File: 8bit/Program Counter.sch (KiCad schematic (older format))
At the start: 7 parts

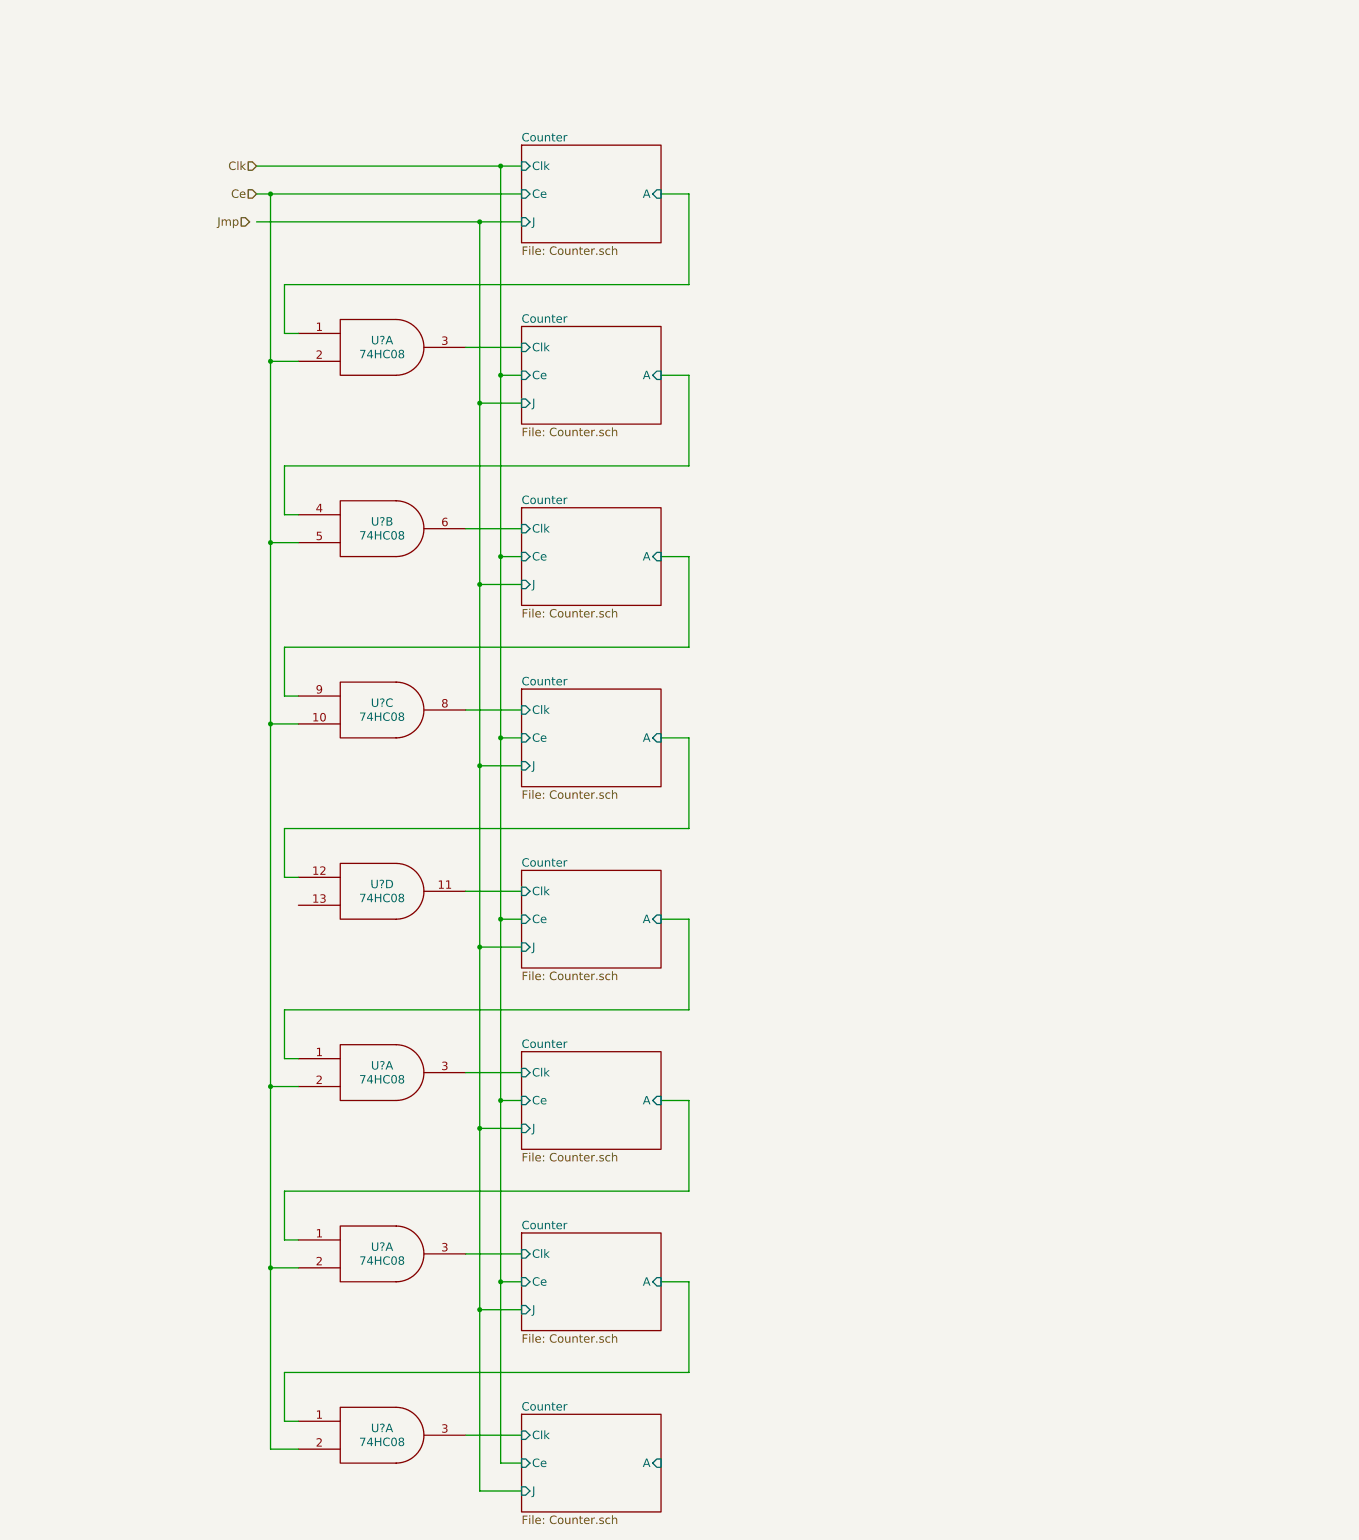
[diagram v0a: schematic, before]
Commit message: Counter mux in progress
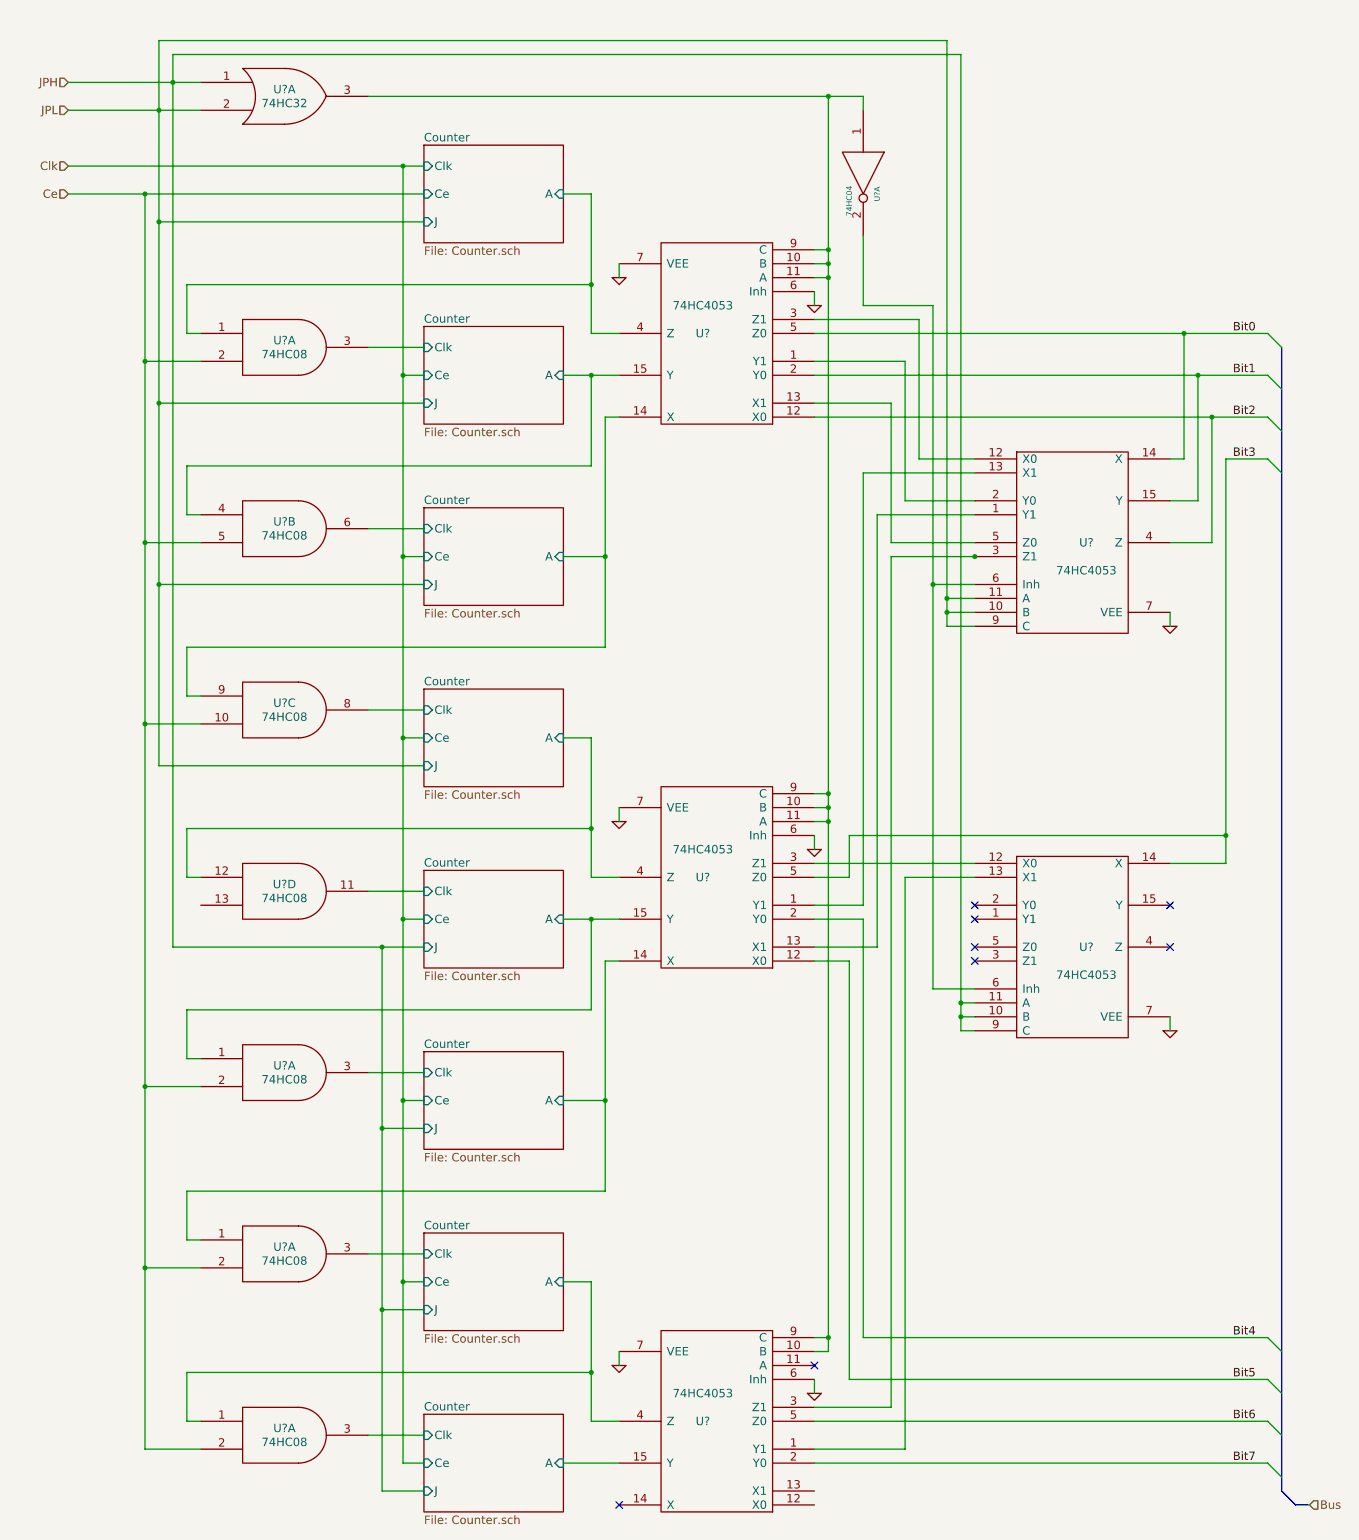
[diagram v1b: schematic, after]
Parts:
- added U?: 74HC32, symbol 74HC32
- added U?: 74HC04, symbol 74HC04
- added U? (x5): 74HC4053, symbol 74HC4053
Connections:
- net Counter/Clk is gone; now on net Counter/Clk: U?.3
- net Counter/A: now also U?.15 (Y) (x3)
- net Counter/Clk: no longer U?.3
- net GND: now also U?.6 (Inh), U?.6 (Inh), U?.6 (Inh), U?.7 (GND), U?.7 (GND), U?.7 (VEE), U?.7 (VEE), U?.7 (VEE), U?.7 (VEE), U?.7 (VEE)
- net VCC: now also U?.14 (VCC), U?.14 (VCC)
- net Counter/A: now also U?.4 (Z) (x3)
- net Counter/A: now also U?.14 (X) (x2)
- new net: U?.1, U?.10 (B), U?.10 (B), U?.10 (B), U?.11 (A), U?.11 (A), U?.3, U?.9 (C), U?.9 (C), U?.9 (C)
- new net: U?.2, U?.6 (Inh), U?.6 (Inh)
- new net: U?.1 (Y1), U?.13 (X1) (x3)
- new net: U?.12 (X0), U?.3 (Z1) (x2)
- new net: U?.1 (Y1), U?.2 (Y0)
- new net: U?.13 (X1), U?.5 (Z0)
- new net: U?.3 (Z1), U?.3 (Z1)
- new net Bit0: U?.14 (X), U?.5 (Z0)
- new net Bit1: U?.15 (Y), U?.2 (Y0)
- new net Bit2: U?.12 (X0), U?.4 (Z)
- new net Bit3: U?.14 (X), U?.5 (Z0)
- new net Bit4: U?.2 (Y0)
- new net Bit5: U?.12 (X0)
- new net Bit6: U?.5 (Z0)
- new net Bit7: U?.2 (Y0)
- new net Counter/Clk: U?.3
- new net JPH: U?.1, U?.10 (B), U?.11 (A), U?.9 (C)
- new net JPL: U?.10 (B), U?.11 (A), U?.2, U?.9 (C)
- new net VDD: U?.16 (VDD), U?.16 (VDD), U?.16 (VDD), U?.16 (VDD), U?.16 (VDD)
- new net VSS: U?.8 (VSS), U?.8 (VSS), U?.8 (VSS), U?.8 (VSS), U?.8 (VSS)
- no-connect marks 0 -> 8
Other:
- moved on the sheet: U?A, U?B, U?C, U?D

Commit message: Added tri-state buffer functionality to counter
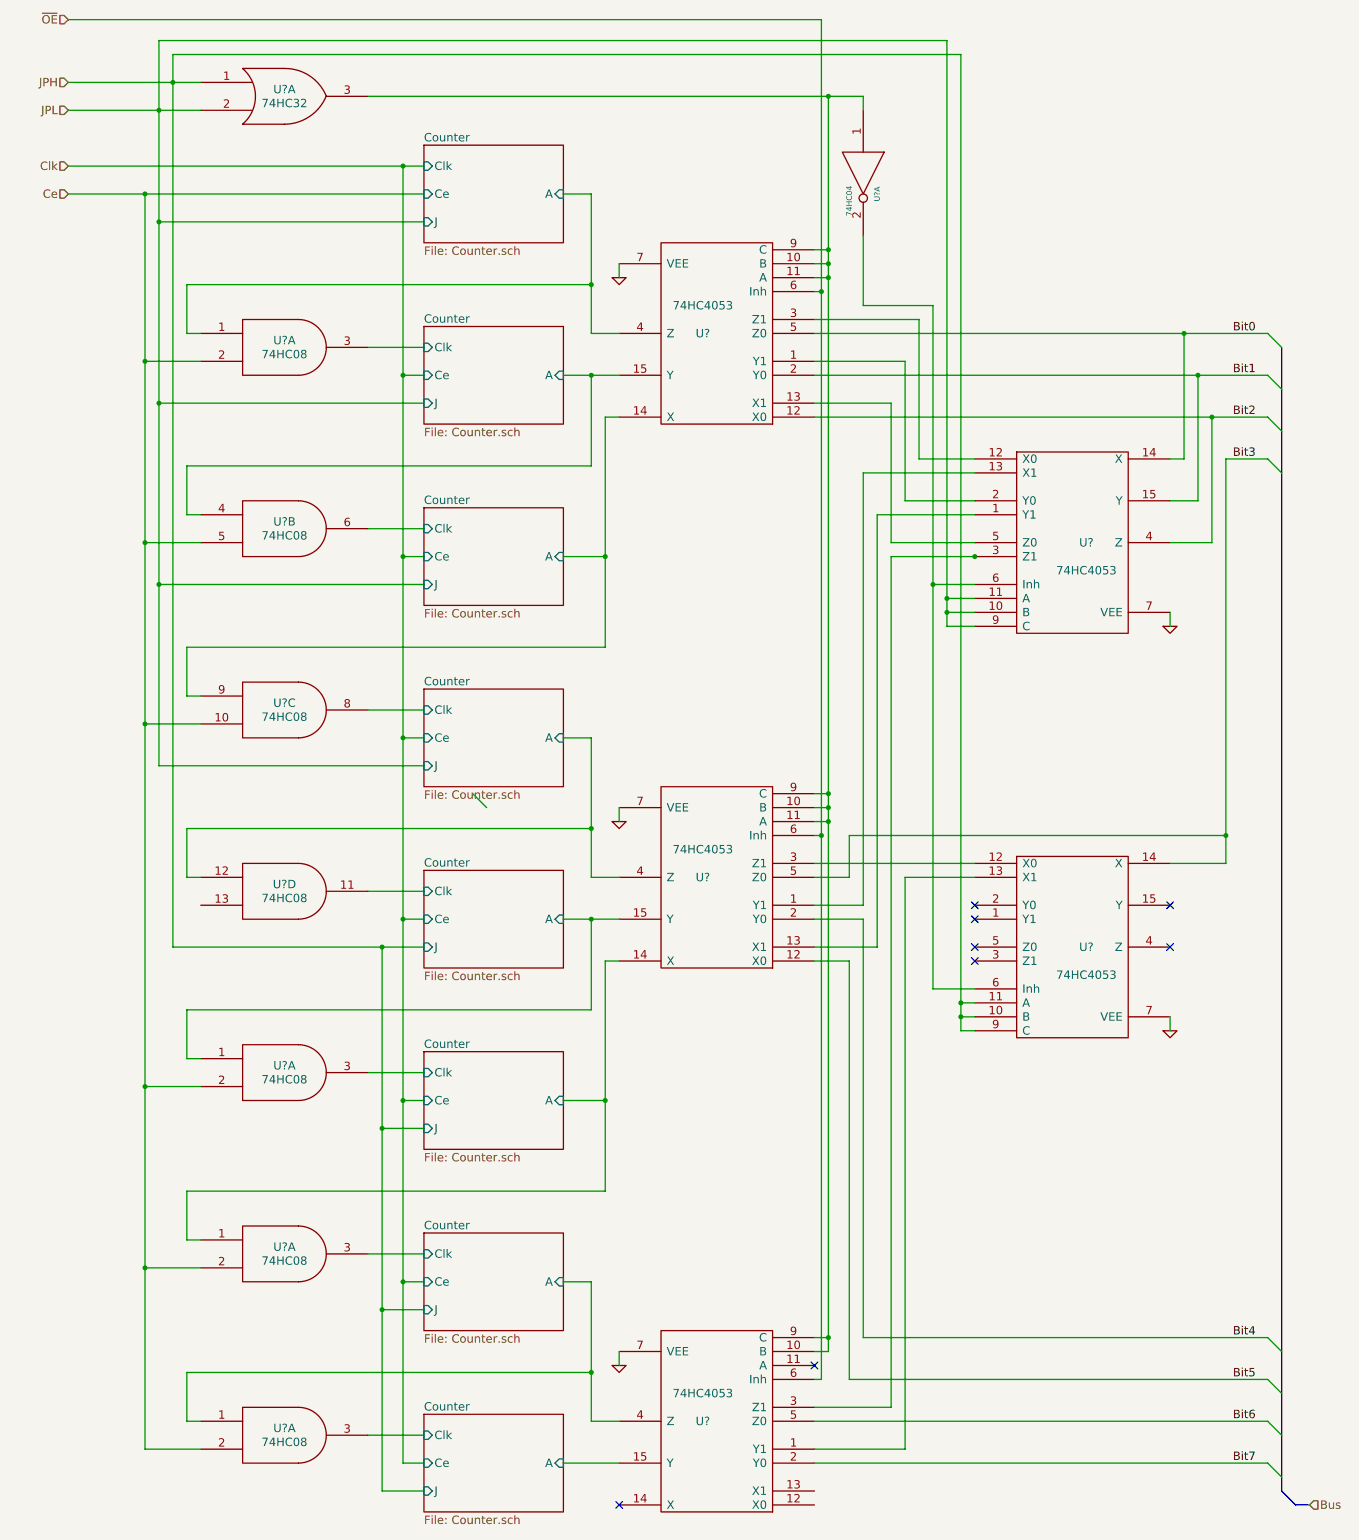
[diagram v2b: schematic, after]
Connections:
- net Counter/A is gone; now on net Counter/A: U?.15 (Y)
- net Counter/Clk is gone; now on net Counter/Clk: U?.3
- net Counter/A: no longer U?.1, U?.4 (Z)
- net Counter/Clk: no longer U?.3
- net GND: no longer U?.6 (Inh), U?.6 (Inh), U?.6 (Inh)
- new net Counter/A: U?.1, U?.4 (Z)
- new net Counter/Clk: U?.3
- new net ~OE: U?.6 (Inh), U?.6 (Inh), U?.6 (Inh)
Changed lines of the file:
@@
 $EndComp
 Wire Wire Line
-	4800 2400 4800 3400
+	4800 2400 4800 3050
+Wire Wire Line
+	4800 3050 4800 3400
 Wire Wire Line
 	4800 3050 1900 3050
@@
 	3200 4800 3600 4800
 Wire Wire Line
-	4900 4000 4900 5650
+	4900 4000 4900 5000
+Wire Wire Line
+	4900 5000 4900 5650
 Wire Wire Line
 	4900 5650 1900 5650
@@
 	3200 6100 3600 6100
 Wire Wire Line
-	1050 2400 3600 2400
+	1050 2400 1600 2400
+Wire Wire Line
+	1600 2400 3600 2400
 Wire Wire Line
 	2000 3600 1600 3600
 Wire Wire Line
-	1600 2400 1600 11400
+	1600 2400 1600 3600
+Wire Wire Line
+	1600 3600 1600 4900
+Wire Wire Line
+	1600 4900 1600 6200
+Wire Wire Line
+	1600 6200 1600 8800
+Wire Wire Line
+	1600 8800 1600 10100
+Wire Wire Line
+	1600 10100 1600 11400
 Connection ~ 1600 2400
 Wire Wire Line
@@
 Connection ~ 1600 4900
 Wire Wire Line
-	1050 2200 3600 2200
-Wire Wire Line
-	3450 2200 3450 11500
+	1050 2200 3450 2200
+Wire Wire Line
+	3450 2200 3600 2200
+Wire Wire Line
+	3450 2200 3450 3700
+Wire Wire Line
+	3450 3700 3450 5000
+Wire Wire Line
+	3450 5000 3450 6300
+Wire Wire Line
+	3450 6300 3450 7600
+Wire Wire Line
+	3450 7600 3450 8900
+Wire Wire Line
+	3450 8900 3450 10200
+Wire Wire Line
+	3450 10200 3450 11500
 Wire Wire Line
 	3450 6300 3600 6300
@@
 	1900 8600 2000 8600
 Wire Wire Line
-	4900 7900 4900 9550
+	4900 7900 4900 8900
+Wire Wire Line
+	4900 8900 4900 9550
 Wire Wire Line
 	4900 9550 1900 9550
@@
 	3200 10000 3600 10000
 Wire Wire Line
-	4800 10200 4800 11200
+	4800 10200 4800 10850
+Wire Wire Line
+	4800 10850 4800 11200
 Wire Wire Line
 	4800 10850 1900 10850
@@
 Connection ~ 3450 6300
 Wire Wire Line
-	4800 6300 4800 7300
+	4800 6300 4800 6950
+Wire Wire Line
+	4800 6950 4800 7300
 Wire Wire Line
 	4800 6950 1900 6950
@@
 Connection ~ 3450 7600
 Wire Wire Line
-	1800 7800 3600 7800
+	1800 7800 3300 7800
+Wire Wire Line
+	3300 7800 3600 7800
 Connection ~ 3300 7800
 Connection ~ 4800 3700
@@
 	4600 8900 4900 8900
 Wire Wire Line
-	4600 7600 5000 7600
+	4600 7600 4800 7600
+Wire Wire Line
+	4800 7600 5000 7600
 Wire Wire Line
 	4800 7300 5000 7300
@@
 	4600 5000 4900 5000
 Wire Wire Line
-	4600 3700 5000 3700
+	4600 3700 4800 3700
+Wire Wire Line
+	4800 3700 5000 3700
 Wire Wire Line
 	4800 3400 5000 3400
@@
 	6750 10600 9650 10600
 Wire Wire Line
-	6400 3400 9650 3400
-Wire Wire Line
-	6400 3700 9650 3700
-Wire Wire Line
-	6400 4000 9650 4000
+	6400 3400 9050 3400
+Wire Wire Line
+	9050 3400 9650 3400
+Wire Wire Line
+	6400 3700 9150 3700
+Wire Wire Line
+	9150 3700 9650 3700
+Wire Wire Line
+	6400 4000 9250 4000
+Wire Wire Line
+	9250 4000 9650 4000
 Wire Wire Line
 	6400 3300 7150 3300
@@
 	9350 4300 9650 4300
 Wire Wire Line
-	9350 4300 9350 7200
+	9350 4300 9350 7000
+Wire Wire Line
+	9350 7000 9350 7200
 Connection ~ 9350 7000
 Wire Wire Line
@@
 	6950 5000 6950 11100
 Wire Bus Line
-	9750 3500 9750 11700
+	9750 3500 9750 3800
+Wire Bus Line
+	9750 3800 9750 4100
+Wire Bus Line
+	9750 4100 9750 4400
+Wire Bus Line
+	9750 4400 9750 10700
+Wire Bus Line
+	9750 10700 9750 11000
+Wire Bus Line
+	9750 11000 9750 11300
+Wire Bus Line
+	9750 11300 9750 11600
+Wire Bus Line
+	9750 11600 9750 11700
 Wire Bus Line
 	9750 11700 9850 11800
@@
 	9850 11800 9950 11800
 Wire Wire Line
-	1050 1600 2000 1600
-Wire Wire Line
-	1050 1800 2000 1800
-Wire Wire Line
-	3200 1700 6750 1700
-Wire Wire Line
-	3300 7800 3300 11700
-Wire Wire Line
-	1800 1400 1800 7800
+	1050 1600 1800 1600
+Wire Wire Line
+	1800 1600 2000 1600
+Wire Wire Line
+	1050 1800 1700 1800
+Wire Wire Line
+	1700 1800 2000 1800
+Wire Wire Line
+	3200 1700 6500 1700
+Wire Wire Line
+	6500 1700 6750 1700
+Wire Wire Line
+	3300 7800 3300 9100
+Wire Wire Line
+	3300 9100 3300 10400
+Wire Wire Line
+	3300 10400 3300 11700
+Wire Wire Line
+	1800 1400 1800 1600
+Wire Wire Line
+	1800 1600 1800 7800
 Connection ~ 1800 1600
 Wire Wire Line
 	1700 3900 3600 3900
 Wire Wire Line
-	1700 1300 1700 6500
+	1700 1300 1700 1800
+Wire Wire Line
+	1700 1800 1700 2600
+Wire Wire Line
+	1700 2600 1700 3900
+Wire Wire Line
+	1700 3900 1700 5200
+Wire Wire Line
+	1700 5200 1700 6500
 Connection ~ 1700 1800
 Wire Wire Line
@@
 	7450 8400 7550 8400
 Wire Wire Line
-	7450 1400 7450 8400
+	7450 1400 7450 8200
+Wire Wire Line
+	7450 8200 7450 8300
+Wire Wire Line
+	7450 8300 7450 8400
 Wire Wire Line
 	7450 1400 1800 1400
@@
 	1700 1300 7350 1300
 Wire Wire Line
-	7350 1300 7350 5500
+	7350 1300 7350 5300
+Wire Wire Line
+	7350 5300 7350 5400
+Wire Wire Line
+	7350 5400 7350 5500
 Wire Wire Line
 	7350 5500 7550 5500
@@
 Connection ~ 7450 8200
 Wire Wire Line
-	6500 1700 6500 10700
+	6500 1700 6500 2800
+Wire Wire Line
+	6500 2800 6500 2900
+Wire Wire Line
+	6500 2900 6500 3000
+Wire Wire Line
+	6500 3000 6500 6700
+Wire Wire Line
+	6500 6700 6500 6800
+Wire Wire Line
+	6500 6800 6500 6900
+Wire Wire Line
+	6500 6900 6500 10600
+Wire Wire Line
+	6500 10600 6500 10700
 Wire Wire Line
 	6500 3000 6400 3000
@@
 	6400 6700 6500 6700
 Connection ~ 6500 6700
-$Comp
-L GND #PWR?
-U 1 1 549B45AF
-P 6400 3200
-F 0 "#PWR?" H 6400 3200 30  0001 C CNN
-F 1 "GND" H 6400 3130 30  0001 C CNN
-F 2 "" H 6400 3200 60  0000 C CNN
-F 3 "" H 6400 3200 60  0000 C CNN
-	1    6400 3200
-	1    0    0    -1
-$EndComp
-Wire Wire Line
-	6400 3200 6400 3100
-$Comp
-L GND #PWR?
-U 1 1 549B47CE
-P 6400 7100
-F 0 "#PWR?" H 6400 7100 30  0001 C CNN
-F 1 "GND" H 6400 7030 30  0001 C CNN
-F 2 "" H 6400 7100 60  0000 C CNN
-F 3 "" H 6400 7100 60  0000 C CNN
-	1    6400 7100
-	1    0    0    -1
-$EndComp
-Wire Wire Line
-	6400 7100 6400 7000
 Wire Wire Line
 	6500 10700 6400 10700
@@
 	6400 10600 6500 10600
 Connection ~ 6500 10600
-$Comp
-L GND #PWR?
-U 1 1 549B5D6A
-P 6400 11000
-F 0 "#PWR?" H 6400 11000 30  0001 C CNN
-F 1 "GND" H 6400 10930 30  0001 C CNN
-F 2 "" H 6400 11000 60  0000 C CNN
-F 3 "" H 6400 11000 60  0000 C CNN
-	1    6400 11000
-	1    0    0    -1
-$EndComp
-Wire Wire Line
-	6400 11000 6400 10900
 NoConn ~ 6400 10800
 NoConn ~ 5000 11800
@@
 	7250 8100 7550 8100
 Wire Wire Line
-	7250 3200 7250 8100
+	7250 3200 7250 5200
+Wire Wire Line
+	7250 5200 7250 8100
 Connection ~ 7250 5200
 $Comp
@@
 Connection ~ 6500 1700
 Connection ~ 7550 5000
+Entry Wire Line
+	3950 6700 4050 6800
+Text HLabel 1050 1150 0    60   Input ~ 0
+~OE
+Wire Wire Line
+	1050 1150 6450 1150
+Wire Wire Line
+	6450 1150 6450 3100
+Wire Wire Line
+	6450 3100 6450 7000
+Wire Wire Line
+	6450 7000 6450 10900
+Wire Wire Line
+	6450 10900 6400 10900
+Wire Wire Line
+	6400 7000 6450 7000
+Connection ~ 6450 7000
+Wire Wire Line
+	6400 3100 6450 3100
+Connection ~ 6450 3100
 $EndSCHEMATC

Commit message: Created 16:8 mux sheet for simplicity
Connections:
- net Counter/A is gone; now on net Counter/A: U?.15 (Y)
- net Counter/Clk is gone; now on net Counter/Clk: U?.3
- net Counter/A: no longer U?.1, U?.4 (Z)
- net Counter/Clk: no longer U?.3
- new net Counter/A: U?.1, U?.4 (Z)
- new net Counter/Clk: U?.3
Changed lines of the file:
@@
 $Descr A3 11693 16535 portrait
 encoding utf-8
-Sheet 15 27
+Sheet 15 28
 Title ""
 Date ""

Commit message: Created 8-bit NAND Sheet, added to ALU
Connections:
- net Counter/A is gone; now on net Counter/A: U?.15 (Y)
- net Counter/Clk is gone; now on net Counter/Clk: U?.3
- net Counter/A: no longer U?.1, U?.4 (Z)
- net Counter/Clk: no longer U?.3
- new net Counter/A: U?.1, U?.4 (Z)
- new net Counter/Clk: U?.3
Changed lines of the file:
@@
 $Descr A3 11693 16535 portrait
 encoding utf-8
-Sheet 15 28
+Sheet 15 29
 Title ""
 Date ""

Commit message: Added Comparator to ALU, removed NAND
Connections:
- net Counter/A is gone; now on net Counter/A: U?.15 (Y)
- net Counter/Clk is gone; now on net Counter/Clk: U?.3
- net Counter/A: no longer U?.1, U?.4 (Z)
- net Counter/Clk: no longer U?.3
- new net Counter/A: U?.1, U?.4 (Z)
- new net Counter/Clk: U?.3
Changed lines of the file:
@@
 $Descr A3 11693 16535 portrait
 encoding utf-8
-Sheet 15 29
+Sheet 15 28
 Title ""
 Date ""
